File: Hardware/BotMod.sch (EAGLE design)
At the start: 39 parts, among them Q1 BSS138, Q2 BSS138, T1 MMBT2222A, U1 LSM303D

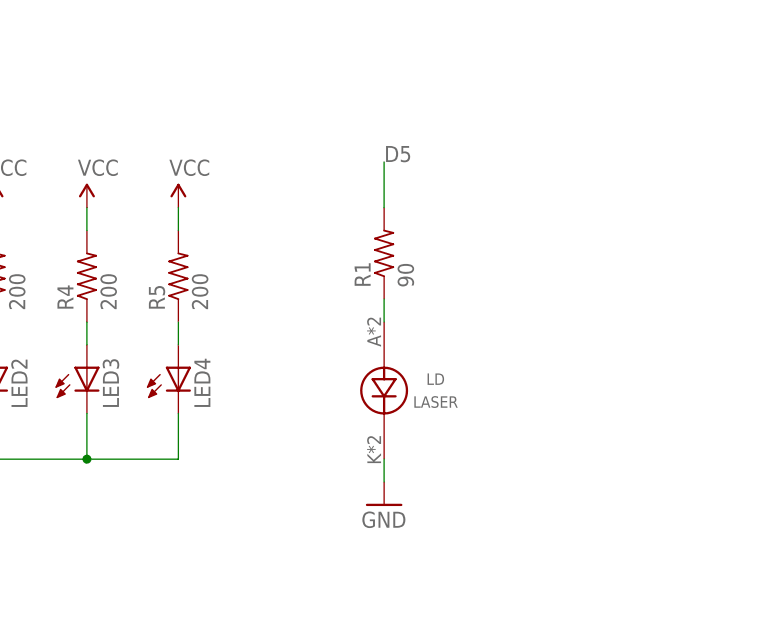
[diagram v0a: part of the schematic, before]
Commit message: Laser resistor removed
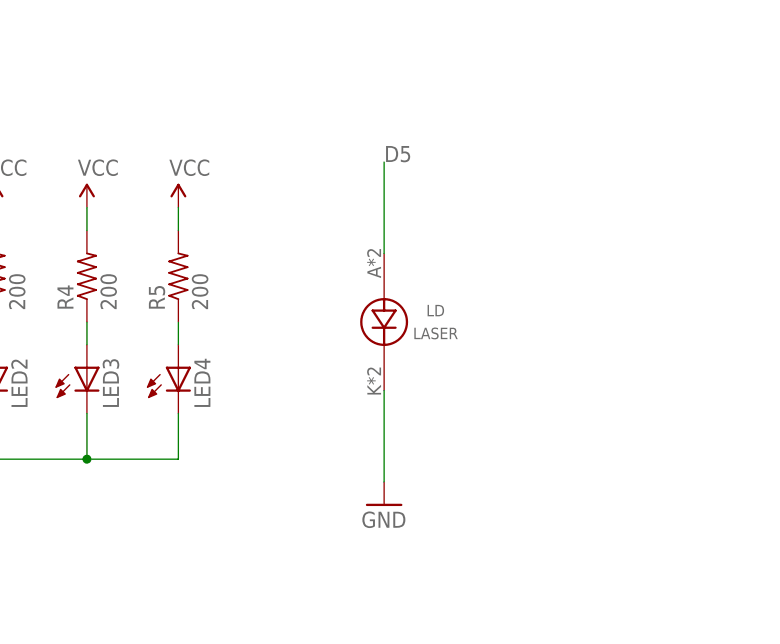
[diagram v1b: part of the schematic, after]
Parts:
- removed R1: 90, resistor:R-US_R1206
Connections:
- removed net N$9: LD.A, R1.1
- net D5: now also LD.A; no longer R1.2
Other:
- moved on the sheet: LD
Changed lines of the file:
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@@
 <part name="GND6" library="SparkFun" deviceset="GND" device=""/>
 <part name="LD" library="SpaceDIY" deviceset="KEYES_LASER" device="" value="LASER"/>
-<part name="R1" library="resistor" deviceset="R-US_" device="R1206" value="90"/>
 <part name="GND7" library="SparkFun" deviceset="GND" device=""/>
 <part name="U1" library="LSM303D" deviceset="LSM303D" device=""/>
@@
 <instance part="R8" gate="G$1" x="139.7" y="66.04" rot="R180"/>
 <instance part="GND6" gate="1" x="152.4" y="50.8"/>
-<instance part="LD" gate="G$1" x="223.52" y="58.42"/>
-<instance part="R1" gate="G$1" x="223.52" y="73.66" rot="R90"/>
+<instance part="LD" gate="G$1" x="223.52" y="66.04"/>
 <instance part="GND7" gate="1" x="223.52" y="45.72"/>
 <instance part="U1" gate="G$1" x="60.96" y="99.06" rot="MR0"/>
@@
 <pinref part="LD" gate="G$1" pin="K"/>
 <pinref part="GND7" gate="1" pin="GND"/>
-<wire x1="223.52" y1="48.26" x2="223.52" y2="50.8" width="0.1524" layer="91"/>
+<wire x1="223.52" y1="48.26" x2="223.52" y2="58.42" width="0.1524" layer="91"/>
 </segment>
 <segment>
@@
 </segment>
 <segment>
-<pinref part="R1" gate="G$1" pin="2"/>
-<wire x1="223.52" y1="78.74" x2="223.52" y2="83.82" width="0.1524" layer="91"/>
+<wire x1="223.52" y1="73.66" x2="223.52" y2="83.82" width="0.1524" layer="91"/>
 <label x="223.52" y="83.82" size="1.778" layer="95"/>
+<pinref part="LD" gate="G$1" pin="A"/>
 </segment>
 </net>
@@
 </segment>
 </net>
-<net name="N$9" class="0">
-<segment>
-<pinref part="LD" gate="G$1" pin="A"/>
-<pinref part="R1" gate="G$1" pin="1"/>
-<wire x1="223.52" y1="68.58" x2="223.52" y2="66.04" width="0.1524" layer="91"/>
-</segment>
-</net>

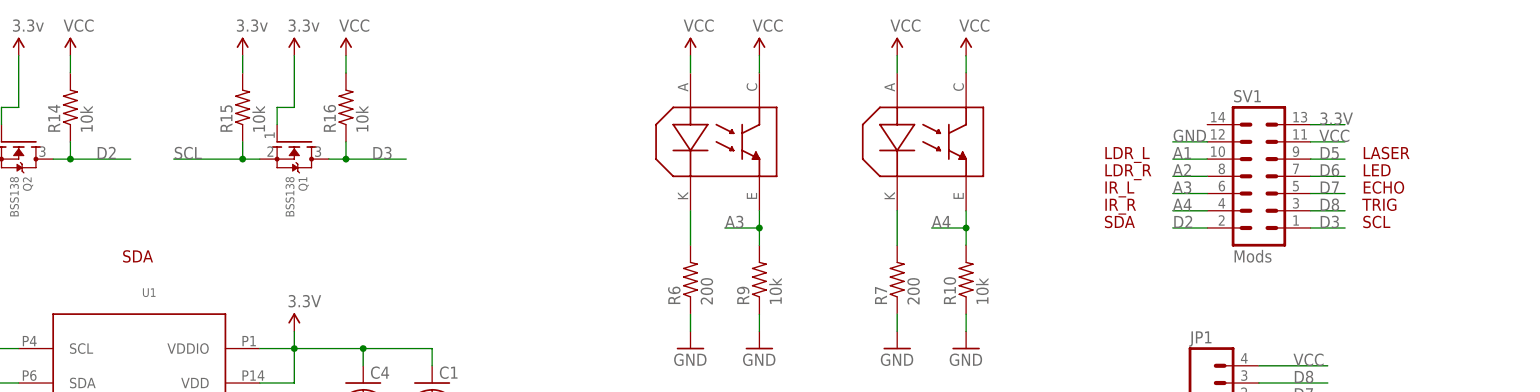
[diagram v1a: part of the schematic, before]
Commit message: Mod connector updated to 16 pin
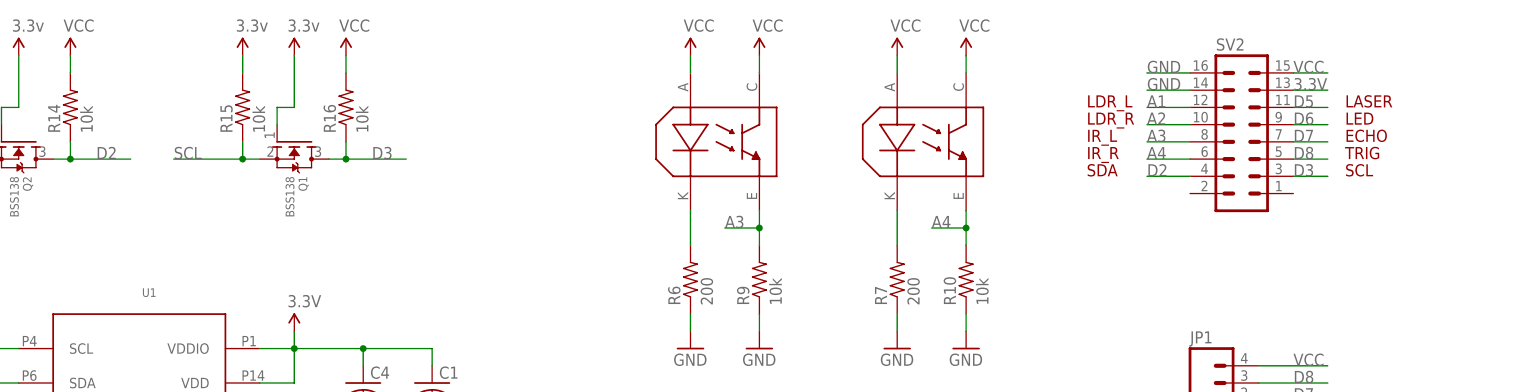
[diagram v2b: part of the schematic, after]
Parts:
- removed SV1: Mods, con-lstb:MA07-2
- added SV2: (no value), con-lstb:MA08-2
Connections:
- net 3.3V: now also SV2.13; no longer SV1.13
- net A1: now also SV2.12; no longer SV1.10
- net A2: now also SV2.10; no longer SV1.8
- net A3: now also SV2.8; no longer SV1.6
- net A4: now also SV2.6; no longer SV1.4
- net D2: now also SV2.4; no longer SV1.2
- net D3: now also SV2.3; no longer SV1.1
- net D5: now also SV2.11; no longer SV1.9
- net D6: now also SV2.9; no longer SV1.7
- net D7: now also SV2.7; no longer SV1.5
- net D8: now also SV2.5; no longer SV1.3
- net GND: now also SV2.14, SV2.16; no longer SV1.12
- net VCC: now also SV2.15; no longer SV1.11

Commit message: SCH and BRD updated Production Files (GERBER, BOM and Centroid)
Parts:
- removed R16: 10k, resistor:R-US_R1206
- added R1: 200, resistor:R-US_R1206
- R7: value 200 -> 1k
- R8: value 1k -> 10k
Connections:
- net D3: now also R8.1; no longer R16.1
- net D6: now also R7.2; no longer R8.2
- net GND: now also R1.1; no longer R7.1
- net N$2: now also R7.1; no longer R8.1
- net N$4: now also R1.2; no longer R7.2
- net VCC: now also R8.2; no longer R16.2
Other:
- moved on the sheet: R7, R8
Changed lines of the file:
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@@
 <part name="R10" library="resistor" deviceset="R-US_" device="R1206" value="10k"/>
 <part name="R6" library="resistor" deviceset="R-US_" device="R1206" value="200"/>
-<part name="R7" library="resistor" deviceset="R-US_" device="R1206" value="200"/>
+<part name="R1" library="resistor" deviceset="R-US_" device="R1206" value="200"/>
 <part name="P+2" library="SparkFun" deviceset="3.3V" device="" value="VCC"/>
 <part name="P+3" library="SparkFun" deviceset="3.3V" device="" value="VCC"/>
@@
 <part name="P+10" library="SparkFun" deviceset="3.3V" device="" value="VCC"/>
 <part name="T1" library="transistor" deviceset="*-NPN-" device="SOT23-BEC" technology="BC808" value="MMBT2222A"/>
-<part name="R8" library="resistor" deviceset="R-US_" device="R1206" value="1k"/>
+<part name="R7" library="resistor" deviceset="R-US_" device="R1206" value="1k"/>
 <part name="GND6" library="SparkFun" deviceset="GND" device=""/>
 <part name="LD" library="SpaceDIY" deviceset="KEYES_LASER" device="" value="LASER"/>
@@
 <part name="Q1" library="adafruit" deviceset="MOSFET-N" device="REFLOW" value="BSS138"/>
 <part name="R15" library="resistor" deviceset="R-US_" device="R1206" value="10k"/>
-<part name="R16" library="resistor" deviceset="R-US_" device="R1206" value="10k"/>
+<part name="R8" library="resistor" deviceset="R-US_" device="R1206" value="10k"/>
 <part name="3.3V6" library="SparkFun" deviceset="3.3V" device="" value="3.3v"/>
 <part name="P+11" library="SparkFun" deviceset="3.3V" device="" value="VCC"/>
@@
 <instance part="R10" gate="G$1" x="182.88" y="127" rot="R90"/>
 <instance part="R6" gate="G$1" x="142.24" y="127" rot="R90"/>
-<instance part="R7" gate="G$1" x="172.72" y="127" rot="R90"/>
+<instance part="R1" gate="G$1" x="172.72" y="127" rot="R90"/>
 <instance part="P+2" gate="G$1" x="142.24" y="160.02"/>
 <instance part="P+3" gate="G$1" x="152.4" y="160.02"/>
@@
 <instance part="P+10" gate="G$1" x="200.66" y="78.74"/>
 <instance part="T1" gate="G$1" x="149.86" y="66.04"/>
-<instance part="R8" gate="G$1" x="139.7" y="66.04" rot="R180"/>
+<instance part="R7" gate="G$1" x="139.7" y="66.04" rot="R180"/>
 <instance part="GND6" gate="1" x="152.4" y="50.8"/>
 <instance part="LD" gate="G$1" x="223.52" y="66.04"/>
@@
 <instance part="Q1" gate="G$1" x="83.82" y="147.32" rot="R270"/>
 <instance part="R15" gate="G$1" x="76.2" y="152.4" rot="R90"/>
-<instance part="R16" gate="G$1" x="91.44" y="152.4" rot="R90"/>
+<instance part="R8" gate="G$1" x="91.44" y="152.4" rot="R90"/>
 <instance part="3.3V6" gate="G$1" x="76.2" y="160.02"/>
 <instance part="P+11" gate="G$1" x="91.44" y="160.02"/>
@@
 </segment>
 <segment>
-<pinref part="R7" gate="G$1" pin="1"/>
+<pinref part="R1" gate="G$1" pin="1"/>
 <pinref part="GND4" gate="1" pin="GND"/>
 <wire x1="172.72" y1="119.38" x2="172.72" y2="121.92" width="0.1524" layer="91"/>
@@
 <wire x1="91.44" y1="157.48" x2="91.44" y2="160.02" width="0.1524" layer="91"/>
 <pinref part="P+11" gate="G$1" pin="3.3V"/>
-<pinref part="R16" gate="G$1" pin="2"/>
+<pinref part="R8" gate="G$1" pin="2"/>
 </segment>
 <segment>
@@
 <pinref part="Q1" gate="G$1" pin="D"/>
 <wire x1="88.9" y1="144.78" x2="91.44" y2="144.78" width="0.1524" layer="91"/>
-<pinref part="R16" gate="G$1" pin="1"/>
+<pinref part="R8" gate="G$1" pin="1"/>
 <wire x1="100.33" y1="144.78" x2="91.44" y2="144.78" width="0.1524" layer="91"/>
 <wire x1="91.44" y1="144.78" x2="91.44" y2="147.32" width="0.1524" layer="91"/>
@@
 <net name="D6" class="0">
 <segment>
-<pinref part="R8" gate="G$1" pin="2"/>
+<pinref part="R7" gate="G$1" pin="2"/>
 <wire x1="134.62" y1="66.04" x2="127" y2="66.04" width="0.1524" layer="91"/>
 <label x="127" y="66.04" size="1.778" layer="95"/>
@@
 <segment>
 <pinref part="IR2" gate="G$1" pin="K"/>
-<pinref part="R7" gate="G$1" pin="2"/>
+<pinref part="R1" gate="G$1" pin="2"/>
 <wire x1="172.72" y1="132.08" x2="172.72" y2="137.16" width="0.1524" layer="91"/>
 </segment>
@@
 <segment>
 <pinref part="T1" gate="G$1" pin="B"/>
-<pinref part="R8" gate="G$1" pin="1"/>
+<pinref part="R7" gate="G$1" pin="1"/>
 <wire x1="144.78" y1="66.04" x2="147.32" y2="66.04" width="0.1524" layer="91"/>
 </segment>

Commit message: Update
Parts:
- added JP2, JP3: (no value), pinhead:PINHD-1X3
- added S1: DPDT_JS202011CQN, bt_electromech:DPDT_JS202011CQN
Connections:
- new net LAS: LD.A, S1.R1
- new net LED: R7.2, S1.L1
- new net S1: JP2.1, S1.L2
- new net S2: JP3.1, S1.R2
- net D5: now also S1.RC; no longer LD.A
- net D6: now also S1.LC; no longer R7.2
- net GND: now also JP2.3, JP3.3
- net VCC: now also JP2.2, JP3.2
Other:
- note added: "LASER/S2"
- note added: "LED/S1"
- note removed: "LASER"
- note removed: "LED"
- moved on the sheet: LD, LED1, LED2, LED3, LED4, R2, R3, R4, R5, R7, T1

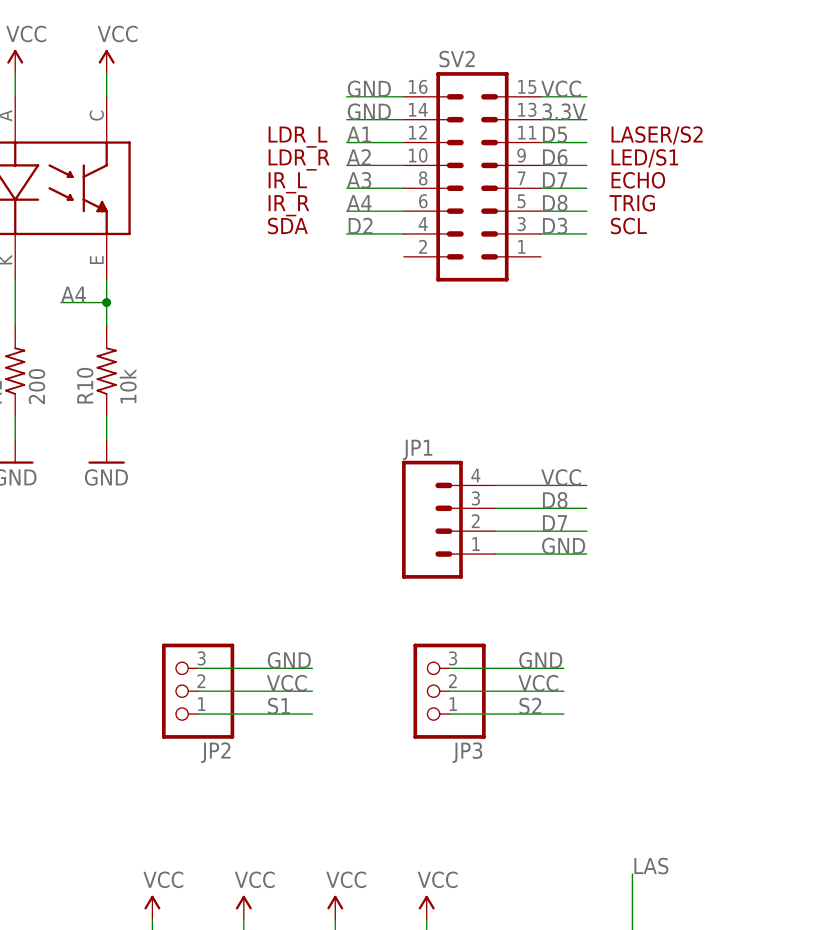
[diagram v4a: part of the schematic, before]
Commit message: Updated design files: - Added support for GPS through Serial port - Silkscreen layouts improved
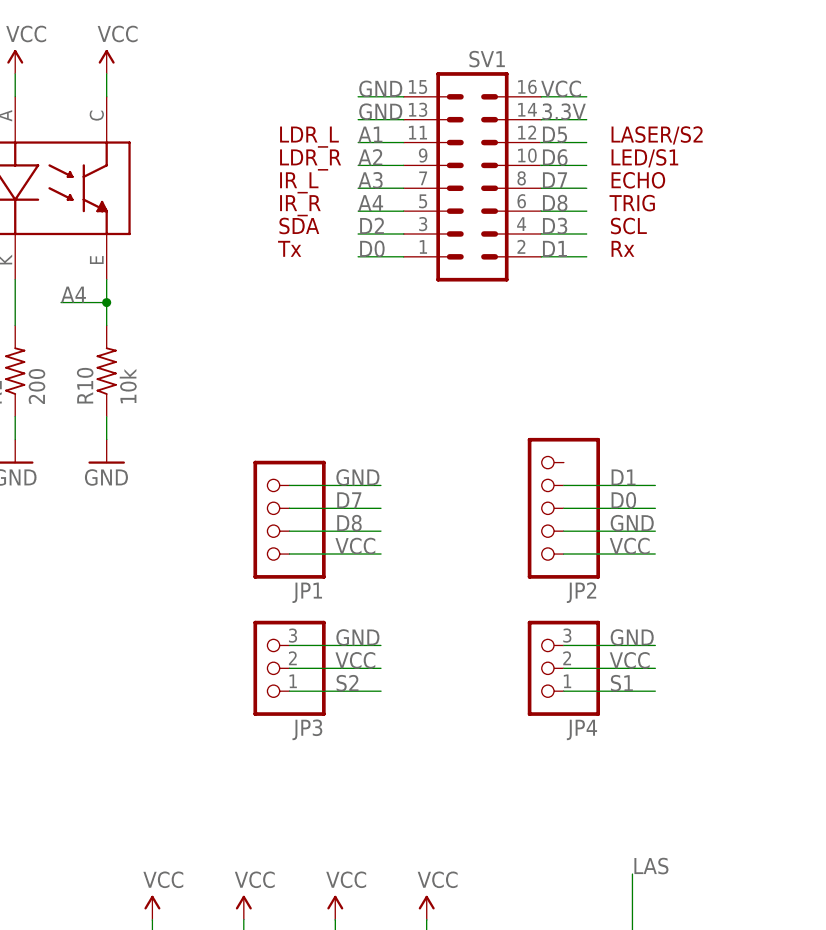
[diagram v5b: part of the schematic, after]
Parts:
- added JP4: (no value), pinhead:PINHD-1X3
- JP1: value (none) -> PINHEAD_4_FEMALE; device SparkFun-Connectors:M04SMD_RA_FEMALE -> SpaceDIY_connectors:PINHEAD_4_FEMALE
- JP2: value (none) -> PINHEAD_5_FEMALE; device pinhead:PINHD-1X3 -> SpaceDIY_connectors:PINHEAD_5_FEMALE
- renumbered SV2 to SV1
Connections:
- new net D0: JP2.3, SV1.1
- new net D1: JP2.4, SV1.2
- net 3.3V: now also SV1.14; no longer SV1.13
- net A1: now also SV1.11; no longer SV1.12
- net A2: now also SV1.9; no longer SV1.10
- net A3: now also SV1.7; no longer SV1.8
- net A4: now also SV1.5; no longer SV1.6
- net D2: now also SV1.3; no longer SV1.4
- net D3: now also SV1.4; no longer SV1.3
- net D5: now also SV1.12; no longer SV1.11
- net D6: now also SV1.10; no longer SV1.9
- net D7: now also JP1.3, SV1.8; no longer JP1.2, SV1.7
- net D8: now also JP1.2, SV1.6; no longer JP1.3, SV1.5
- net GND: now also JP1.4, JP2.2, JP4.3, SV1.13, SV1.15; no longer JP1.1, JP2.3, SV1.14, SV1.16
- net S1: now also JP4.1; no longer JP2.1
- net VCC: now also JP1.1, JP2.1, JP4.2, SV1.16; no longer JP1.4, JP2.2, SV1.15
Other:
- note added: "Rx"
- note added: "Tx"
- moved on the sheet: JP3
